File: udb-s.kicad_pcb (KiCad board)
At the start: 2 copper layers, 40 x 9 mm, 10 parts, among them J1 TYPE-C-31-M-12, J2 78171-0004

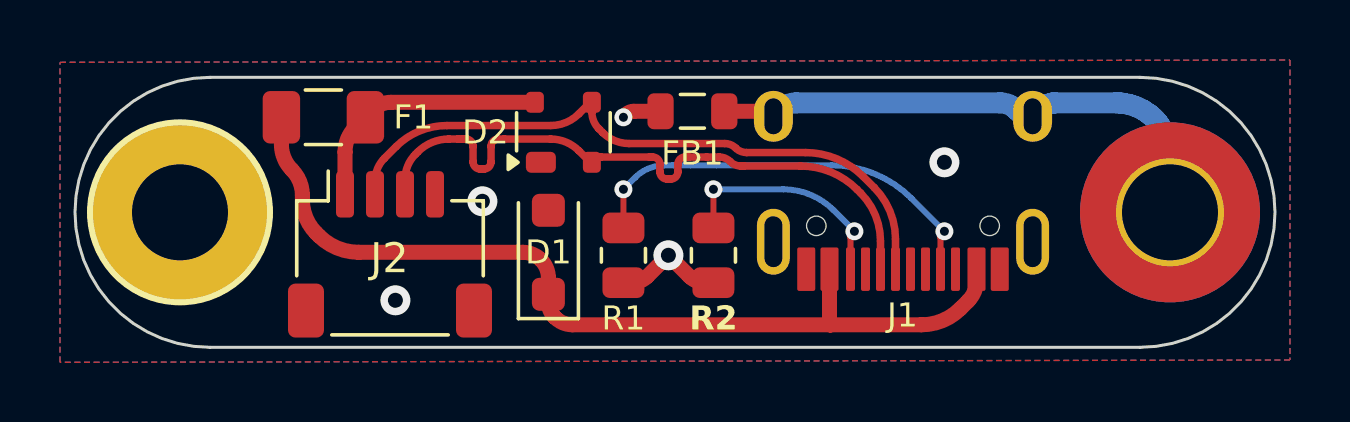
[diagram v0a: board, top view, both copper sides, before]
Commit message: fixed usb traces + teardrops
the usb traces were only connected to two of the pins on the usb connector
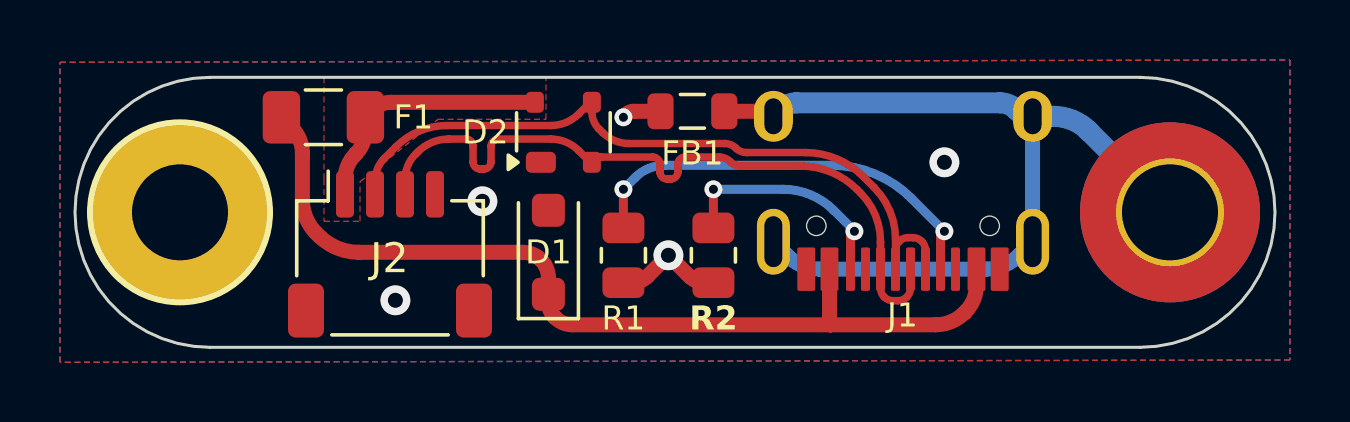
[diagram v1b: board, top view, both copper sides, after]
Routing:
- net GNDPWR: track 18.2 -> 28.9 mm
- net D+: track 22.3 -> 23.9 mm
- net 5V: track 8.61 -> 7.25 mm
- net D-: track 22.4 -> 23.6 mm
- net GND: track 4.99 -> 4.40 mm
- added copper zone on F.Cu, net 5V

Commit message: made production files + BOM
generated the production files and filled out the BOM using lcsc components
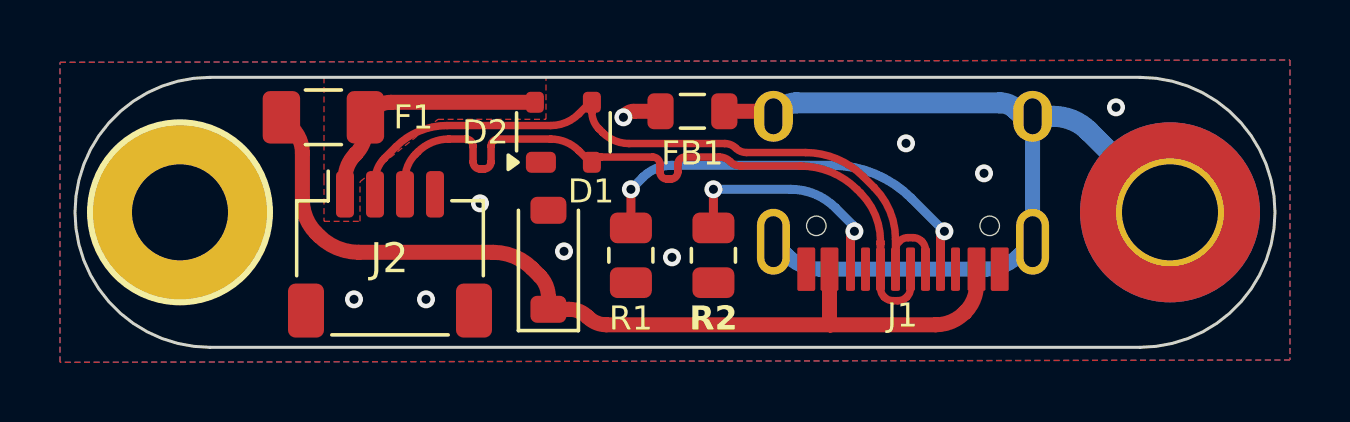
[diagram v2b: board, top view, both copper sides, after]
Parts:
- D1: footprint Diode_SMD:D_SOD-123F -> Diode_SMD:D_SOD-123
- moved D1 0.25 mm to (127.3, 96.6)
- moved R1 0.25 mm to (130.0, 96.4)
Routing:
- net GND: track 4.40 -> 1.30 mm, vias 5 -> 9
- net VBUS: track 31.0 -> 30.2 mm
- net GNDPWR: track 28.9 -> 28.3 mm
- net D+: track 23.9 -> 23.3 mm

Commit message: final tweeks
the USB pair impedance is now closer to 90 and has less interruptions in its reference ground plane
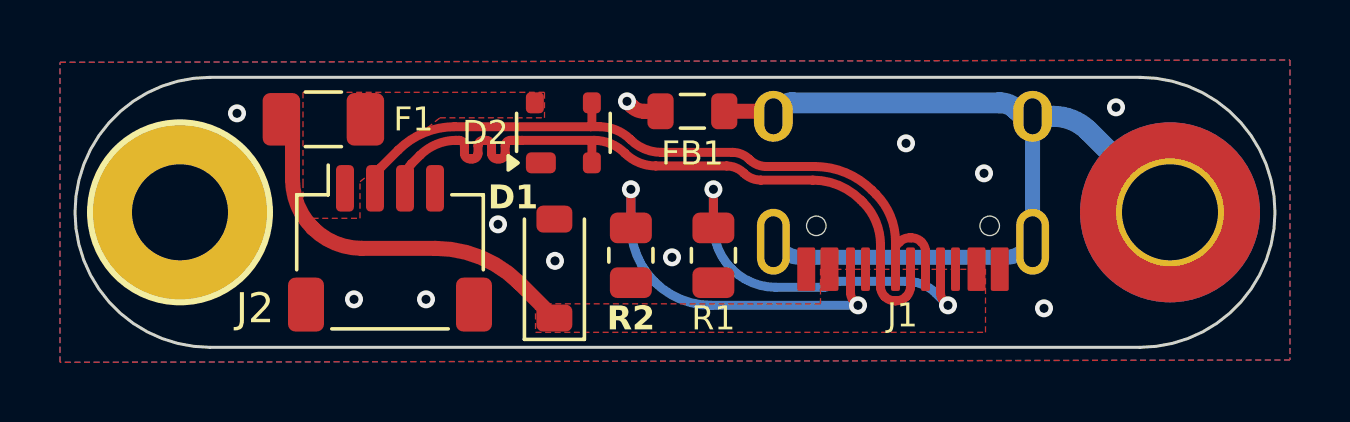
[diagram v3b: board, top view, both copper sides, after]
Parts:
- moved R1 2.75 mm to (132.8, 96.4)
- moved R2 2.75 mm to (130.0, 96.4)
- moved D1 0.35 mm to (127.5, 96.9)
- moved J2 0.20 mm to (122.0, 96.2)
- moved F1 0.07 mm to (119.8, 91.9)
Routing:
- net VBUS: track 30.2 -> 13.2 mm
- net 5V: track 7.25 -> 0.00 mm
- net Net-(J1-CC2): track 7.87 -> 12.8 mm
- net D+: track 23.3 -> 24.3 mm
- net Net-(J1-CC1): track 14.0 -> 13.1 mm
- net GND: track 1.30 -> 1.23 mm, vias 9 -> 11
- added copper zone on F.Cu, net VBUS
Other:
- board text added: "UDB-JST"
- board text added: "you know what cables to use"
- board text removed: "UDB-S with the JST connector with easier to solder and bigger components"
- board text removed: "i hate the molex connector"

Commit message: swapped to SRV05-4
swapped the esd chip to the SRV05-4 and removed the singular diode because its built into the esd chip
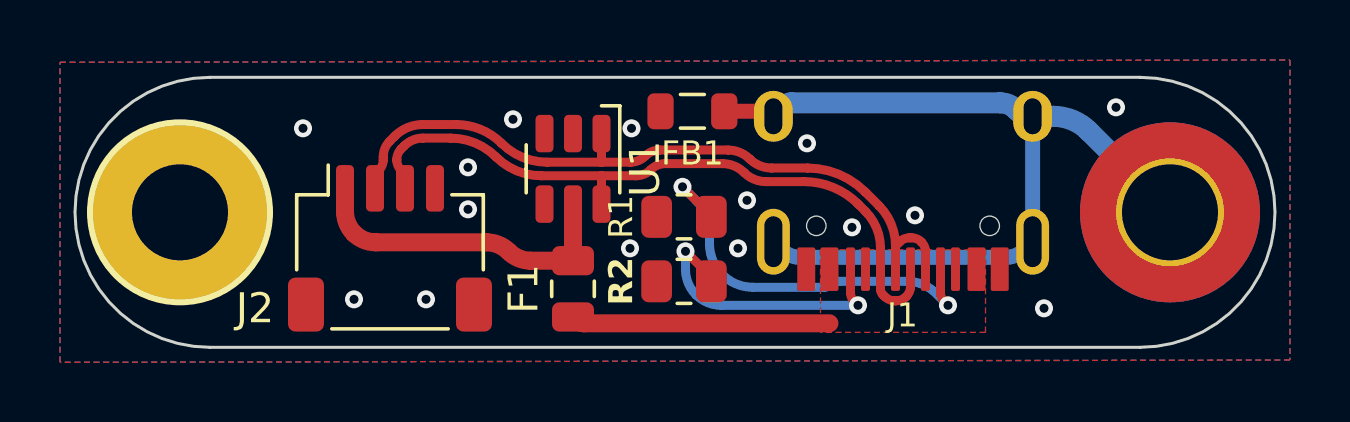
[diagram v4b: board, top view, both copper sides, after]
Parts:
- removed D1: ESD5Z5V0, Diode_SMD:D_SOD-123
- removed D2: PRTR5V0U2X, Package_TO_SOT_SMD:SOT-143
- added U1: SRV05-4, PCM_marbastlib-various:SOT-23-6-routable, F.Cu at (128.1, 93.6)
- F1: footprint Fuse:Fuse_1206_3216Metric -> Fuse:Fuse_0805_2012Metric
- FB1: value GZ2012D601TF -> ~
- J2: value 78171-0004 -> WAFER-SH1.0-4PWB
- moved F1 10.1 mm to (128.1, 97.6), turned to 90 degrees
- moved R2 1.97 mm to (131.8, 97.3), turned to 180 degrees
- moved R1 1.61 mm to (131.8, 95.2), turned to 0 degrees
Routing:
- net 5V: track 0.00 -> 11.0 mm
- net VBUS: track 13.2 -> 8.62 mm
- net Net-(J1-CC2): track 12.8 -> 9.71 mm
- net GND: track 1.23 -> 0.00 mm, vias 11 -> 15
- net Net-(J1-CC1): track 13.1 -> 14.0 mm
- net D+: track 24.3 -> 23.5 mm
- net D-: track 23.7 -> 24.3 mm
- removed copper zone on F.Cu, net 5V

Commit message: usb length matching
made the usb line length matching as well as some other minor stuff
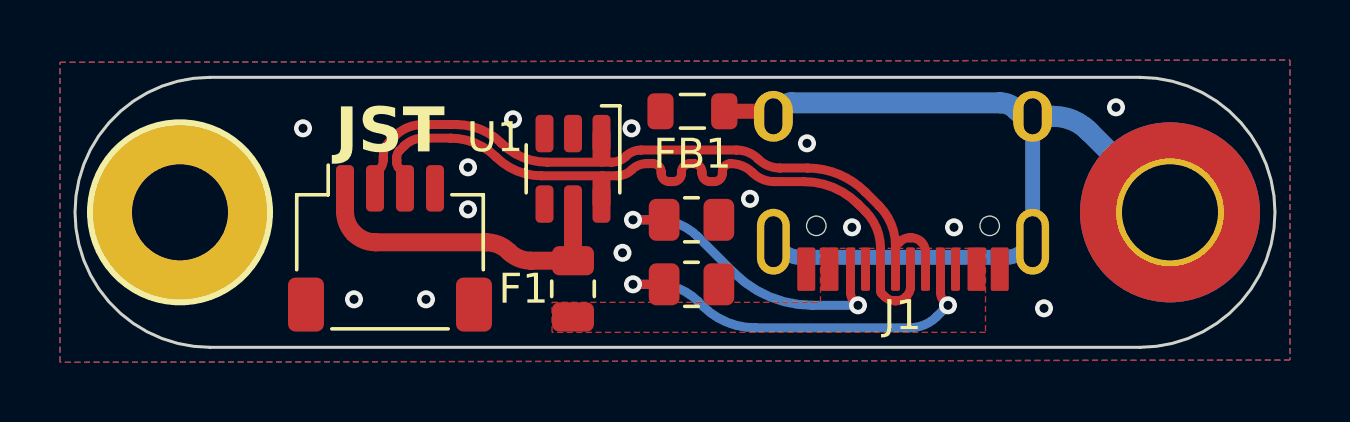
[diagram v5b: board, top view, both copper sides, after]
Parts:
- moved R1 2.26 mm to (132.1, 97.4), turned to 180 degrees
- moved R2 2.07 mm to (132.1, 95.3), turned to 0 degrees
- renumbered J2 to JST
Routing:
- net VBUS: track 8.62 -> 0.00 mm
- net D+: track 23.5 -> 24.8 mm
- net Net-(J1-CC2): track 9.71 -> 10.7 mm
- net Net-(J1-CC1): track 14.0 -> 13.5 mm
- net GND: vias 15 -> 14
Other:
- board text added: "Use UDB Cables"
- board text removed: "you know what cables to use"
